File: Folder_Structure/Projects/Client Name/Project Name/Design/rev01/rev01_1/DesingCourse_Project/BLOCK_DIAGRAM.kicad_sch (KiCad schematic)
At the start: 0 parts

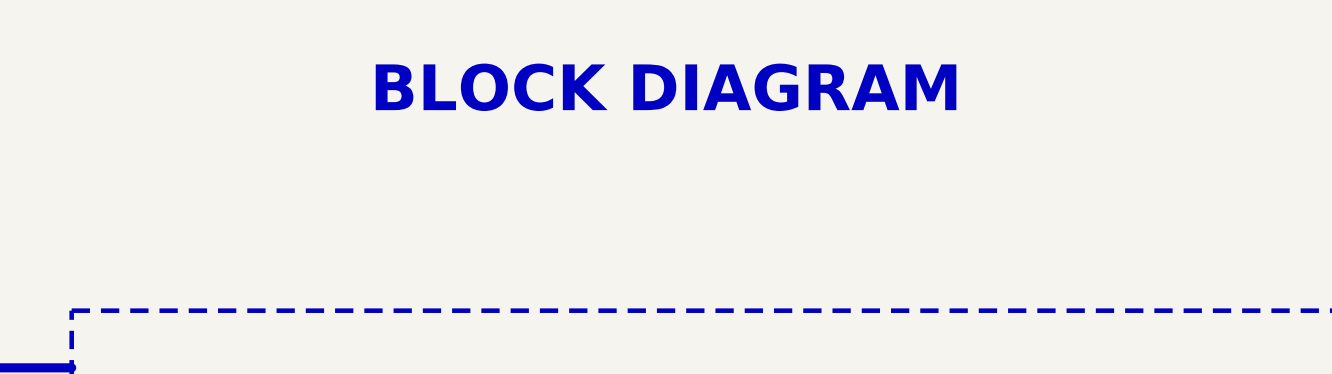
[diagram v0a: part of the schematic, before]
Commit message: Update 4
Finish the MOSFET DRIVE page
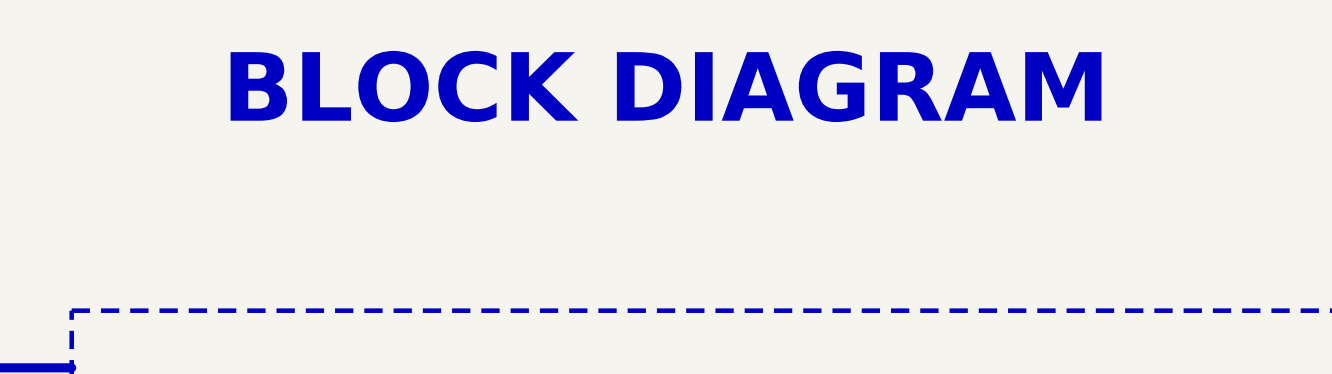
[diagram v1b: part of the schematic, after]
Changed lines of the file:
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@@
 		(effects
 			(font
-				(size 5.08 5.08)
+				(face "Arial Black")
+				(size 7.62 7.62)
 				(thickness 0.254)
 				(bold yes)

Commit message: Update 6
SCH and LIB for MOSFET page done, missing passive components
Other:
- company: (none) -> Integro Consulting AB
- title: (none) -> PCB Mastery Project
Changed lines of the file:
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@@
 	(generator_version "9.0")
 	(paper "A4")
+	(title_block
+		(title "PCB Mastery Project")
+		(date "2026-01-27")
+		(rev "001")
+		(company "Integro Consulting AB")
+		(comment 1 "TBD")
+		(comment 2 "TBD")
+		(comment 3 "TBD")
+		(comment 4 "Josue Godinez")
+	)
 	(text "CAN"
 		(exclude_from_sim no)
